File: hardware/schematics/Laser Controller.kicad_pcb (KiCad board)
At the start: 2 copper layers, 118 x 115 mm, 63 parts, among them J1 Micro_SD_Card, J2 PWR IN +5V, J3 PWR IN Galvo, J4 FAN1 PWR IN, J5 FAN1, J6 FAN2 PWR IN, J7 FAN2, U1 ESP32-S3-N16R8-DevKit, U10 DS18B20, U12 OPA4134UA_2K5, U13 Galvo Input, U15 6N137, U16 6N137, U17 6N137, U2 DAC8562SDGST, U3 TTL_RGB Blue, U4 TTL_RGB Red, U5 TTL_RGB Green, U6 DS18B20, U7 DS18B20, U8 DS18B20, U9 DS18B20

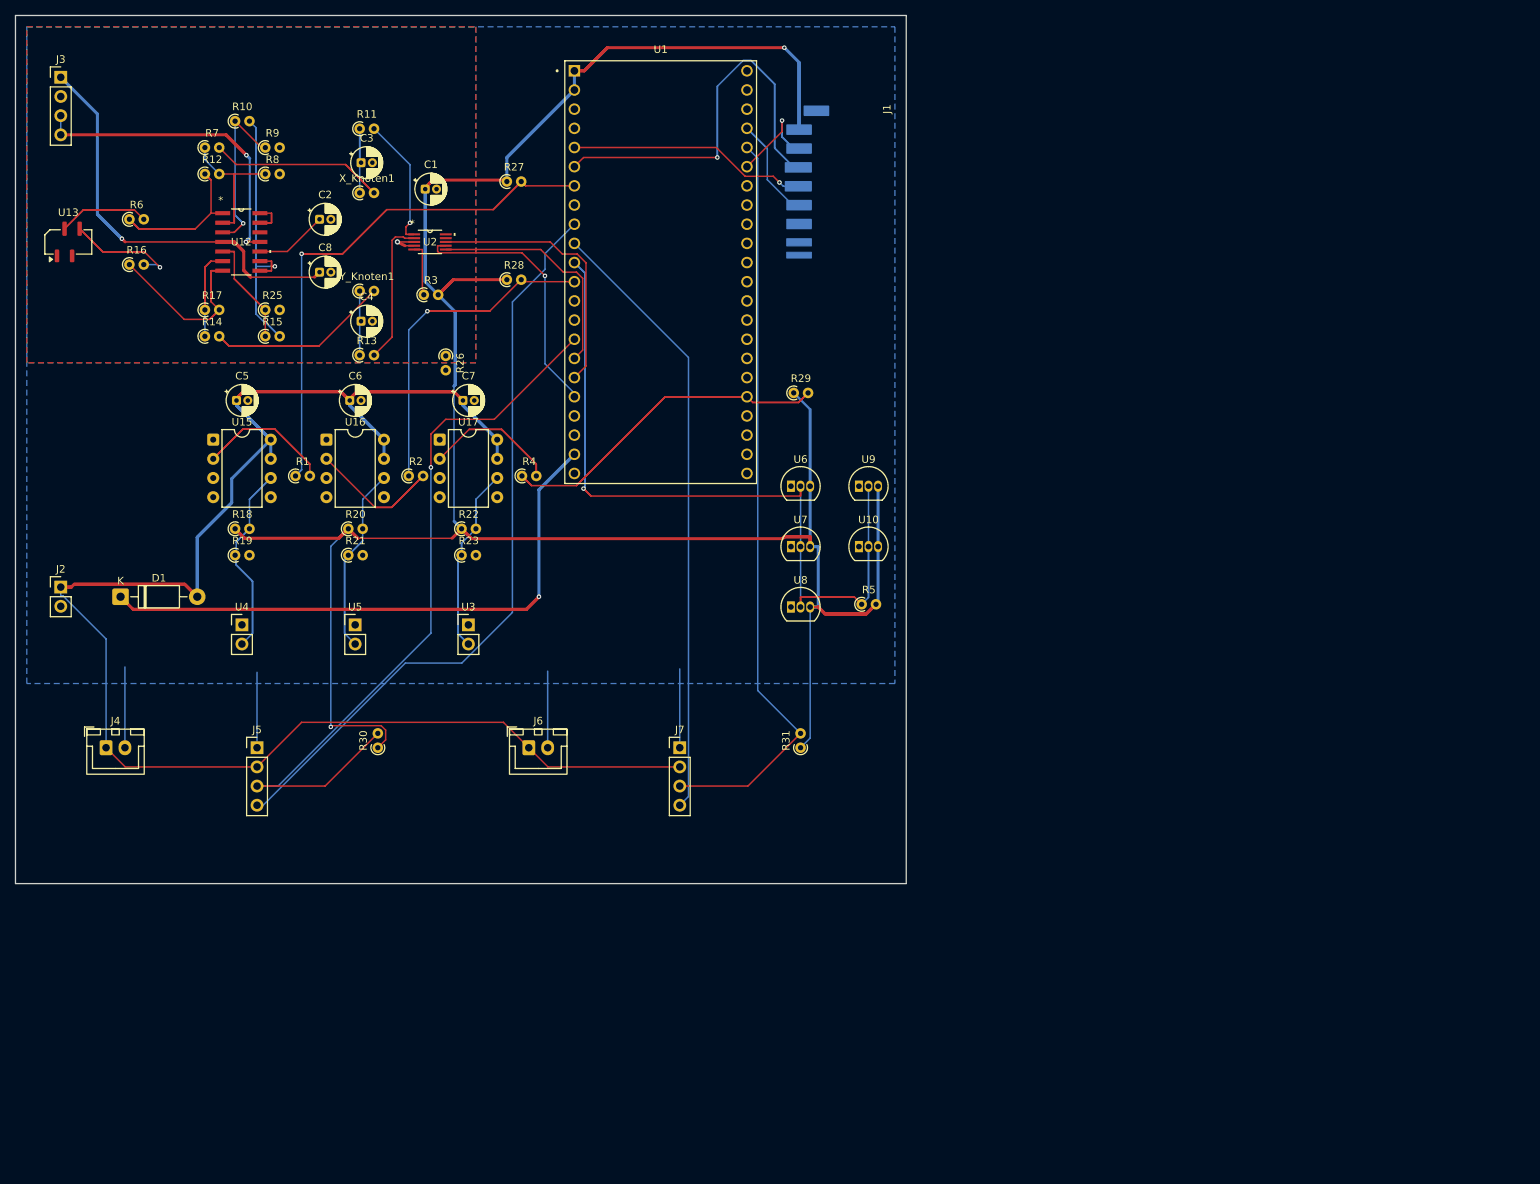
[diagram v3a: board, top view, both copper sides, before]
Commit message: hw: KiCad project catches up on ERC bookkeeping / docs: a caption goes on a diet
Schematic/PCB/project files re-saved after running ERC in KiCad -- pin_map,
erc_exclusions and per-sheet instance data now live in the .kicad_pro, and
the newer format's extra per-symbol fields (do_not_autoplace, show_name,
etc.) landed in the .kicad_sch/.kicad_pcb along the way. No intentional
routing/placement changes.

docs/01-introduction.md's prototype-board photo caption gets trimmed; the
/update page's Chapter 3 walkthrough drops a now-redundant screenshot note.
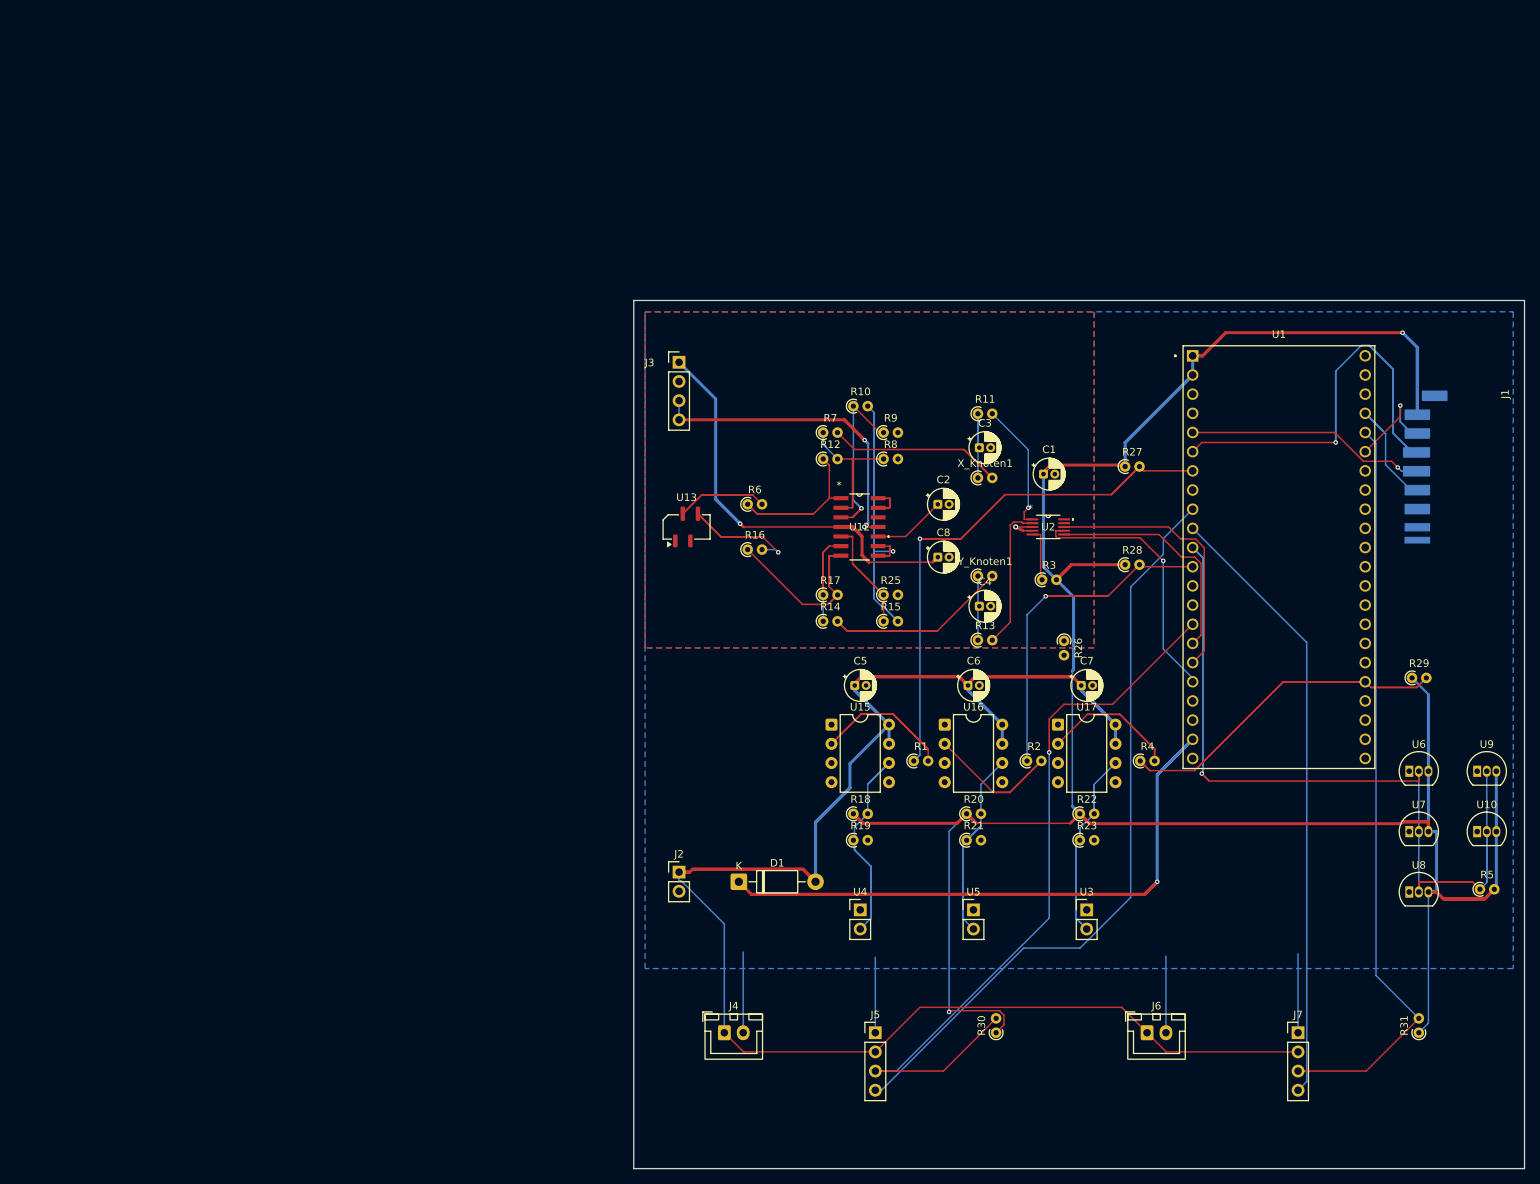
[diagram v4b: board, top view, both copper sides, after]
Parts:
- moved R1 90.2 mm to (119.0, 98.8)
- moved R13 90.2 mm to (127.5, 82.8)
- moved R14 90.2 mm to (107.0, 80.3)
- moved R15 90.2 mm to (115.0, 80.3)
- moved R16 90.2 mm to (97.0, 70.8)
- moved R17 90.2 mm to (107.0, 76.8)
- moved R18 90.2 mm to (111.0, 105.8)
- moved R19 90.2 mm to (111.0, 109.3)
- moved R20 90.2 mm to (126.0, 105.8)
- moved R21 90.2 mm to (126.0, 109.3)
- moved R25 90.2 mm to (115.0, 76.8)
- moved R6 90.2 mm to (97.0, 64.8)
- moved U1 90.2 mm to (167.4, 71.8)
- moved U10 90.2 mm to (193.6, 108.1)
- moved U6 90.2 mm to (184.6, 100.1)
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
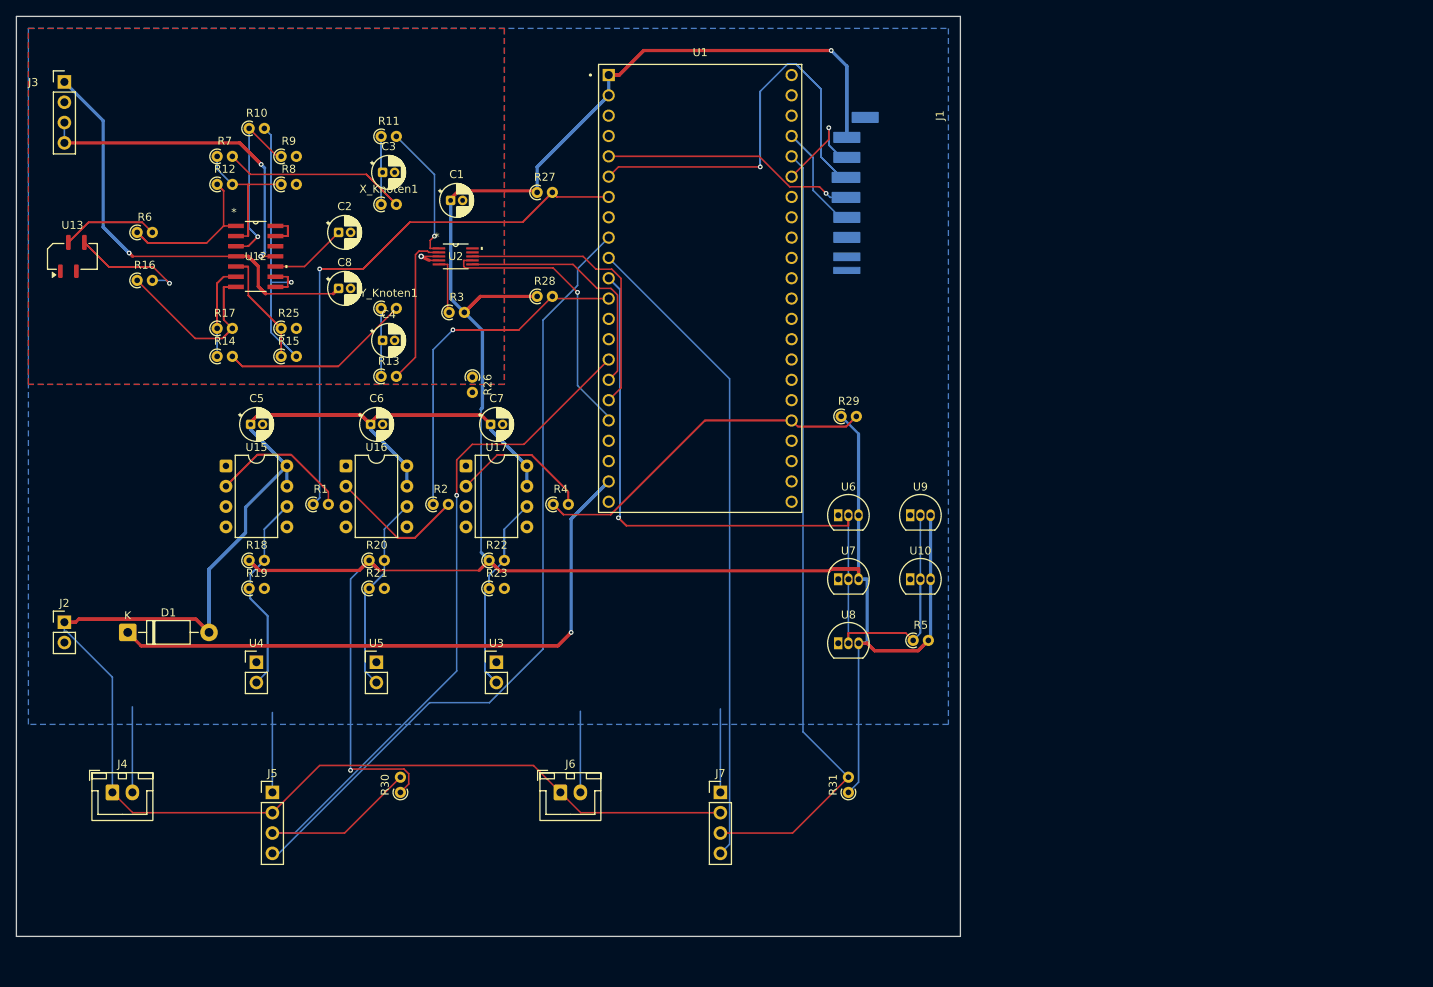
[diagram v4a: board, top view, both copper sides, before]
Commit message: hw: v6.85.0 -- swap DS18B20/RGB/J3 to real JST-XH footprints, not just relabeled ones
- U6-U10 (DS18B20): were still physically the old TO-92 sensor pads
  wearing a JST-XH label (descr/tags still said TO-92). Delete+resync
  from schematic + reposition + reroute -> genuine
  JST_XH_B3B-XH-A_1x03_P2.50mm_Vertical, verified against library.
- U3-U5 (RGB TTL): same bug, same fix -> genuine
  JST_XH_B2B-XH-A_1x02_P2.50mm_Vertical.
- Gave the DS18B20 1-Wire bus an explicit net label (was unnamed,
  which is why pads kept losing their net assignment mid-swap).
- Rewired the 1-Wire + 3V3 daisy chain across all 5 sensors to the
  new pad positions without touching the working legacy trunk.
- J3 (PWR IN Galvo): finished the 3-pin -> 4-pin JST-XH swap properly
  (schematic symbol + footprint), pin 4 wired to -15V.
- ESP32 socket: confirmed the existing devkit footprint IS already a
  proper 2x22 2.54mm THT pin-socket pattern -- added silkscreen note
  + BOM property instead of a needless footprint swap.

Known follow-up: J_DMX and U13 have the same label-only-fix bug,
not yet corrected. DS18B20 column spacing (9mm) is tighter than a
real JST-XH B3B housing needs (~11mm) -- courtyards overlap by
~2x6.8mm, electrically harmless but a real assembly fit issue.

Zero shorts, zero solder-mask bridges, zero missing-net pads on the
touched components; lib_footprint_mismatch confirms U3-U10 now match
the real library parts.
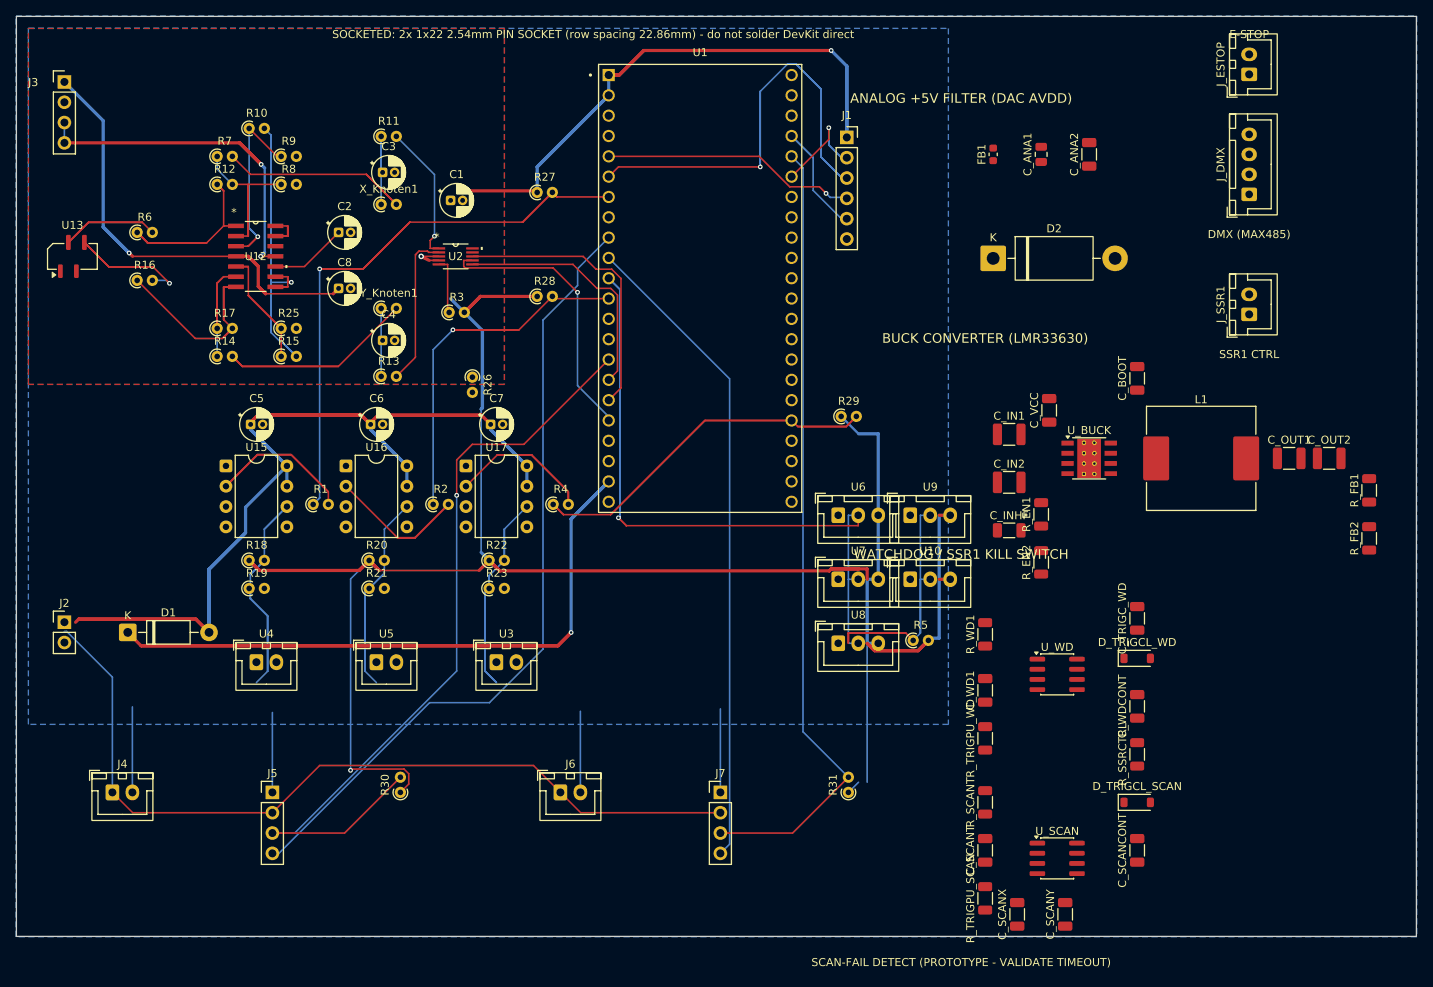
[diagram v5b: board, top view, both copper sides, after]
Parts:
- added C_ANA1: 10uF, Capacitor_SMD:C_0805_2012Metric, F.Cu at (210.0, 55.0)
- added C_ANA2: 100nF, Capacitor_SMD:C_1206_3216Metric, F.Cu at (216.0, 55.0)
- added C_BOOT: 100nF, Capacitor_SMD:C_1206_3216Metric, F.Cu at (222.0, 83.0)
- added C_IN1: 10uF, Capacitor_SMD:C_1210_3225Metric, F.Cu at (206.0, 90.0)
- added C_IN2: 10uF, Capacitor_SMD:C_1210_3225Metric, F.Cu at (206.0, 96.0)
- added C_INHF: 100nF, Capacitor_SMD:C_1206_3216Metric, F.Cu at (206.0, 102.0)
- added C_OUT1: 22uF, Capacitor_SMD:C_1210_3225Metric, F.Cu at (241.0, 93.0)
- added C_OUT2: 22uF, Capacitor_SMD:C_1210_3225Metric, F.Cu at (246.0, 93.0)
- added C_SCANCONT: 10nF, Capacitor_SMD:C_1206_3216Metric, F.Cu at (222.0, 142.0)
- added C_SCANT: 10nF, Capacitor_SMD:C_1206_3216Metric, F.Cu at (203.0, 142.0)
- added C_SCANX: 100nF, Capacitor_SMD:C_1206_3216Metric, F.Cu at (207.0, 150.0)
- added C_SCANY: 100nF, Capacitor_SMD:C_1206_3216Metric, F.Cu at (213.0, 150.0)
- added C_TRIGC_WD: 1nF, Capacitor_SMD:C_1206_3216Metric, F.Cu at (222.0, 113.0)
- added C_VCC: 1uF, Capacitor_SMD:C_1206_3216Metric, F.Cu at (211.0, 87.0)
- added C_WD1: 100nF, Capacitor_SMD:C_1206_3216Metric, F.Cu at (203.0, 122.0)
- added C_WDCONT: 10nF, Capacitor_SMD:C_1206_3216Metric, F.Cu at (222.0, 124.0)
- added D2: 1N5822, Diode_THT:D_DO-201AD_P15.24mm_Horizontal, F.Cu at (204.0, 68.0)
- added D_TRIGCL_SCAN: 1N4148, Diode_SMD:D_SOD-123, F.Cu at (222.0, 136.0)
- added D_TRIGCL_WD: 1N4148, Diode_SMD:D_SOD-123, F.Cu at (222.0, 118.0)
- added FB1: BLM18PG221SN1, Inductor_SMD:L_0603_1608Metric, F.Cu at (204.0, 55.0)
- added J_DMX: DMX MAX485, Connector_PinSocket_2.54mm:PinSocket_1x04_P2.54mm_Vertical, F.Cu at (236.0, 60.0)
- added J_ESTOP: E-STOP, Connector_JST:JST_XH_B2B-XH-A_1x02_P2.50mm_Vertical, F.Cu at (236.0, 45.0)
- added J_SSR1: SSR1 CTRL, Connector_JST:JST_XH_B2B-XH-A_1x02_P2.50mm_Vertical, F.Cu at (236.0, 75.0)
- added L1: 6.8uH, Inductor_SMD:L_Sunlord_MWSA1204S-6R8, F.Cu at (230.0, 93.0)
- added R_EN1: 63.4k 1%, Resistor_SMD:R_1206_3216Metric, F.Cu at (210.0, 100.0)
- added R_EN2: 10k 1%, Resistor_SMD:R_1206_3216Metric, F.Cu at (210.0, 106.0)
- added R_FB1: 100k 1%, Resistor_SMD:R_1206_3216Metric, F.Cu at (251.0, 97.0)
- added R_FB2: 24.9k 1%, Resistor_SMD:R_1206_3216Metric, F.Cu at (251.0, 103.0)
- added R_SCANT: 1.8M, Resistor_SMD:R_1206_3216Metric, F.Cu at (203.0, 136.0)
- added R_SSRCTRL: 330, Resistor_SMD:R_1206_3216Metric, F.Cu at (222.0, 130.0)
- added R_TRIGPU_SCAN: 10k, Resistor_SMD:R_1206_3216Metric, F.Cu at (203.0, 148.0)
- added R_TRIGPU_WD: 10k, Resistor_SMD:R_1206_3216Metric, F.Cu at (203.0, 128.0)
- added R_WD1: 910k 1%, Resistor_SMD:R_1206_3216Metric, F.Cu at (203.0, 115.0)
- added U_BUCK: LMR33630ADDA, Package_SO:Texas_HSOP-8-1EP_3.9x4.9mm_P1.27mm_ThermalVias, F.Cu at (216.0, 93.0)
- added U_SCAN: NE555D, Package_SO:SOIC-8_3.9x4.9mm_P1.27mm, F.Cu at (212.0, 143.0)
- added U_WD: NE555D, Package_SO:SOIC-8_3.9x4.9mm_P1.27mm, F.Cu at (212.0, 120.0)
- J1: value Micro_SD_Card -> SD Card Module (6-pin, 2.54mm); footprint SD_Card_Device_16mm_SlotDepth -> Connector_PinSocket_2.54mm:PinSocket_1x06_P2.54mm_Vertical
- J3: footprint Connector_JST:JST_XH_B3B-XH-A_1x03_P2.50mm_Vertical -> Connector_JST:JST_XH_B4B-XH-A_1x04_P2.50mm_Vertical
- moved J1 14.4 mm to (185.7, 52.9), turned to 0 degrees
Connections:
- net Net-(J1-CLK) renamed SD_SCK
- net Net-(J1-CS) renamed SD_CS
- net Net-(J1-MISO) renamed SD_MISO
- net Net-(J1-MOSI) renamed SD_MOSI
- net Net-(U1-GPIO18) renamed DS18B20_1WIRE
- net Net-(U15-VO) renamed TTL_RGB_RED
- net Net-(U16-VO) renamed TTL_RGB_GREEN
- net Net-(U17-VO) renamed TTL_RGB_BLUE
- C1 pad 1: +3V3 -> +5V_ANA
- J2 pad 1: Buck +5V -> VIN_RAW
- R14 pad 2: Net-(R14-Pad2) -> -15V
- U1 pad J1_20: (no net) -> GPIO14
- U1 pad J1_4: (no net) -> GPIO4
- U1 pad J2_10: (no net) -> GPIO38
- U1 pad J2_17: (no net) -> GPIO47
- U1 pad J2_9: (no net) -> GPIO39
- U2 pad 9: +3V3 -> +5V_ANA
- Y_Knoten1 pad 2: Net-(R14-Pad2) -> -15V
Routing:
- net Net-(R14-Pad2): track 37.8 -> 0.00 mm
- net -15V: track 45.8 -> 83.6 mm
- net +3V3: track 398.9 -> 374.5 mm
- net DS18B20_1WIRE: track 151.1 -> 157.2 mm
- net Buck +5V: track 292.7 -> 288.7 mm
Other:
- board size 118 x 115 mm -> 175 x 115 mm
- board text added: "ANALOG +5V FILTER (DAC AVDD)"
- board text added: "BUCK CONVERTER (LMR33630)"
- board text added: "DMX (MAX485)"
- board text added: "E-STOP"
- board text added: "SCAN-FAIL DETECT (PROTOTYPE - VALIDATE TIMEOUT)"
- board text added: "SOCKETED: 2x 1x22 2.54mm PIN SOCKET (row spacing 22.86mm) - do not solder DevKit direct"
- board text added: "SSR1 CTRL"
- board text added: "WATCHDOG / SSR1 KILL SWITCH"
